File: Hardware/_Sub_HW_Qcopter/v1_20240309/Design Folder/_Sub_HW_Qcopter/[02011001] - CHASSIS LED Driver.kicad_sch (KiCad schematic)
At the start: 2 parts, among them J3201 HDR_1X2_VERT_1.25MM

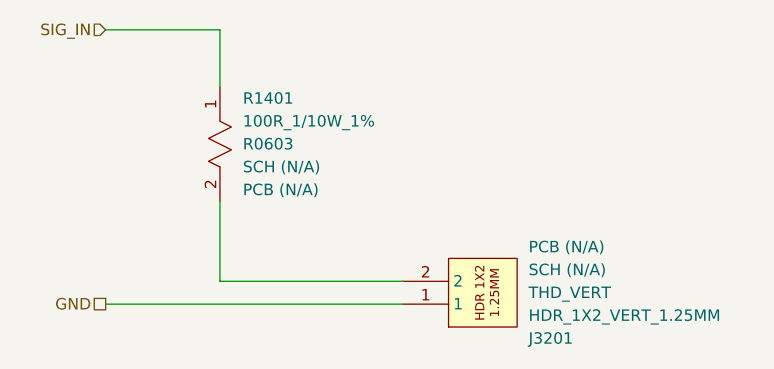
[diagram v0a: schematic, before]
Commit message: Update [02011001] - CHASSIS LED Driver.kicad_sch
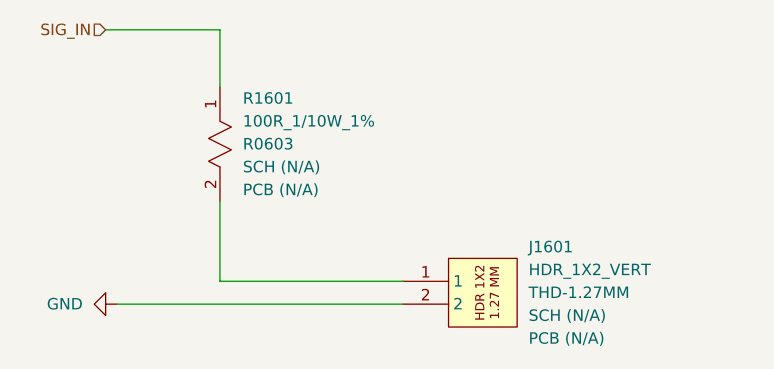
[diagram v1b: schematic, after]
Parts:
- removed J3201: HDR_1X2_VERT_1.25MM, Connector_Hirose:Hirose_DF13-02P-1.25DSA_1x02_P1.25mm_Vertical, symbol _SCHLIB_Qcopter:CONN_HDR_1X2_VERT_THD-1.25MM
- added J1601: HDR_1X2_VERT, Connector_PinHeader_1.27mm:PinHeader_1x02_P1.27mm_Vertical, symbol _SCHLIB_Qcopter:CONN_HDR_1X2_VERT_THD-1.27MM
- renumbered R1401 to R1601
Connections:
- net GND: now also J1601.2
- net at R1601.2: now also J1601.1
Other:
- company: (none) -> Mend0z0
- title: (none) -> Quadcopter
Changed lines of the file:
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@@
 	(paper "C")
 	(title_block
-		(comment 2 "DRAFT")
+		(title "Quadcopter")
+		(date "2024-03-17")
+		(rev "01")
+		(company "Mend0z0")
+		(comment 1 "01")
+		(comment 2 "PRELIMINARY")
+		(comment 3 "Siavash Taher Parvar")
+		(comment 8 "N/A")
+		(comment 9 "First Version")
 	)
 	(wire
@@
 	(wire
 		(pts
-			(xy 241.3 208.28) (xy 274.32 208.28)
+			(xy 254 196.85) (xy 254 205.74)
 		)
 		(stroke
@@
 	(wire
 		(pts
-			(xy 254 196.85) (xy 254 205.74)
+			(xy 241.3 177.8) (xy 254 177.8)
 		)
 		(stroke
@@
 	(wire
 		(pts
-			(xy 241.3 177.8) (xy 254 177.8)
+			(xy 242.57 208.28) (xy 274.32 208.28)
 		)
 		(stroke
 			(width 0)
 			(type default)
-		)
-	)
-	(hierarchical_label "GND"
-		(shape passive)
-		(at 241.3 208.28 180)
-		(fields_autoplaced yes)
-		(effects
-			(font
-				(size 1.27 1.27)
-			)
-			(justify right)
 		)
 	)
@@
 	)
 	(symbol
-		(lib_id "_SCHLIB_Qcopter:CONN_HDR_1X2_VERT_THD-1.25MM")
-		(at 279.4 210.82 0)
-		(mirror x)
+		(lib_id "_SCHLIB_Qcopter:CONN_HDR_1X2_VERT_THD-1.27MM")
+		(at 274.32 205.74 0)
 		(unit 1)
 		(exclude_from_sim no)
@@
 		(on_board yes)
 		(dnp no)
-		(property "Reference" "J3201"
-			(at 288.29 212.0901 0)
-			(effects
-				(font
-					(size 1.27 1.27)
-				)
-				(justify left)
-			)
-		)
-		(property "Value" "HDR_1X2_VERT_1.25MM"
-			(at 288.29 209.5501 0)
-			(effects
-				(font
-					(size 1.27 1.27)
-				)
-				(justify left)
-			)
-		)
-		(property "Footprint" "Connector_Hirose:Hirose_DF13-02P-1.25DSA_1x02_P1.25mm_Vertical"
-			(at 283.21 227.584 0)
-			(effects
-				(font
-					(size 1.27 1.27)
-				)
-				(justify left)
-				(hide yes)
-			)
-		)
-		(property "Datasheet" "https://cdn.amphenol-cs.com/media/wysiwyg/files/documentation/datasheet/boardwiretoboard/bwb_1.25mm_wtb.pdf"
-			(at 282.956 219.964 0)
-			(effects
-				(font
-					(size 1.27 1.27)
-				)
-				(justify left)
-				(hide yes)
-			)
-		)
-		(property "Description" "Connector Header Through Hole 2 position 0.049\" (1.25mm)"
-			(at 282.956 224.79 0)
-			(effects
-				(font
-					(size 1.27 1.27)
-				)
-				(justify left)
-				(hide yes)
-			)
-		)
-		(property "Package" "THD_VERT"
-			(at 288.29 207.0101 0)
-			(effects
-				(font
-					(size 1.27 1.27)
-				)
-				(justify left)
-			)
-		)
-		(property "Part Number (Manufacturer)" "10114829-10102LF"
-			(at 283.21 230.378 0)
-			(effects
-				(font
-					(size 1.27 1.27)
-				)
-				(justify left)
-				(hide yes)
-			)
-		)
-		(property "Manufacturer" "Amphenol ICC (FCI)"
-			(at 283.21 235.204 0)
-			(effects
-				(font
-					(size 1.27 1.27)
-				)
-				(justify left)
-				(hide yes)
-			)
-		)
-		(property "Part Number (Vendor)" "609-4383-2-ND"
-			(at 283.21 232.918 0)
+		(fields_autoplaced yes)
+		(property "Reference" "J1601"
+			(at 288.29 201.9299 0)
+			(effects
+				(font
+					(size 1.27 1.27)
+				)
+				(justify left)
+			)
+		)
+		(property "Value" "HDR_1X2_VERT"
+			(at 288.29 204.4699 0)
+			(effects
+				(font
+					(size 1.27 1.27)
+				)
+				(justify left)
+			)
+		)
+		(property "Footprint" "Connector_PinHeader_1.27mm:PinHeader_1x02_P1.27mm_Vertical"
+			(at 278.13 188.976 0)
+			(effects
+				(font
+					(size 1.27 1.27)
+				)
+				(justify left)
+				(hide yes)
+			)
+		)
+		(property "Datasheet" "https://cdn.harwin.com/pdfs/M50-353.pdf"
+			(at 277.876 196.596 0)
+			(effects
+				(font
+					(size 1.27 1.27)
+				)
+				(justify left)
+				(hide yes)
+			)
+		)
+		(property "Description" "Connector Header Through Hole 2 position 0.050\" (1.27mm)"
+			(at 277.876 191.77 0)
+			(effects
+				(font
+					(size 1.27 1.27)
+				)
+				(justify left)
+				(hide yes)
+			)
+		)
+		(property "Package" "THD-1.27MM"
+			(at 288.29 207.0099 0)
+			(effects
+				(font
+					(size 1.27 1.27)
+				)
+				(justify left)
+			)
+		)
+		(property "Part Number (Manufacturer)" "M50-3530242"
+			(at 278.13 186.182 0)
+			(effects
+				(font
+					(size 1.27 1.27)
+				)
+				(justify left)
+				(hide yes)
+			)
+		)
+		(property "Manufacturer" "Harwin Inc."
+			(at 278.13 181.356 0)
+			(effects
+				(font
+					(size 1.27 1.27)
+				)
+				(justify left)
+				(hide yes)
+			)
+		)
+		(property "Part Number (Vendor)" "952-3598-ND"
+			(at 278.13 183.642 0)
 			(effects
 				(font
@@
 		)
 		(property "Vendor" "Digikey"
-			(at 283.21 237.744 0)
-			(effects
-				(font
-					(size 1.27 1.27)
-				)
-				(justify left)
-				(hide yes)
-			)
-		)
-		(property "Purchase Link" "https://www.digikey.ca/en/products/detail/amphenol-cs-fci/10114829-10102LF/2658929"
-			(at 282.956 222.504 0)
+			(at 278.13 178.816 0)
+			(effects
+				(font
+					(size 1.27 1.27)
+				)
+				(justify left)
+				(hide yes)
+			)
+		)
+		(property "Purchase Link" "https://www.digikey.ca/en/products/detail/harwin-inc/M50-3530242/7044013"
+			(at 277.876 194.056 0)
 			(effects
 				(font
@@
 		)
 		(property "SCH CHECK" "SCH (N/A)"
-			(at 288.29 204.4701 0)
+			(at 288.29 209.5499 0)
 			(effects
 				(font
@@
 		)
 		(property "PCB CHECK" "PCB (N/A)"
-			(at 288.29 201.9301 0)
+			(at 288.29 212.0899 0)
 			(effects
 				(font
@@
 			(project "_Sub_HW_Qcopter"
 				(path "/b8703f06-b3da-4de2-b217-f104939b36e8/6184e84e-040e-4878-8152-76cf0b949e21/e826979f-4a88-401c-bba5-a1c30231907a/18b6f30a-cfd9-47dd-912b-fd9e3d81f3b7/d01f197b-a0f5-41b1-b267-05c3be6c8f44"
-					(reference "J3201")
+					(reference "J1601")
 					(unit 1)
 				)
 				(path "/b8703f06-b3da-4de2-b217-f104939b36e8/6184e84e-040e-4878-8152-76cf0b949e21/e826979f-4a88-401c-bba5-a1c30231907a/18b6f30a-cfd9-47dd-912b-fd9e3d81f3b7/9dfe4c39-4ceb-4fd2-b56a-1baa2fce7dec"
-					(reference "J1401")
+					(reference "J1701")
 					(unit 1)
 				)
 				(path "/b8703f06-b3da-4de2-b217-f104939b36e8/6184e84e-040e-4878-8152-76cf0b949e21/e826979f-4a88-401c-bba5-a1c30231907a/18b6f30a-cfd9-47dd-912b-fd9e3d81f3b7/9b435483-0088-4023-8c4e-fad88eb5f6b4"
-					(reference "J3401")
+					(reference "J1801")
 					(unit 1)
 				)
 				(path "/b8703f06-b3da-4de2-b217-f104939b36e8/6184e84e-040e-4878-8152-76cf0b949e21/e826979f-4a88-401c-bba5-a1c30231907a/18b6f30a-cfd9-47dd-912b-fd9e3d81f3b7/b5f98916-9852-4daa-96f4-3bdba60c13f5"
-					(reference "J3501")
+					(reference "J1901")
+					(unit 1)
+				)
+			)
+		)
+	)
+	(symbol
+		(lib_id "power:GND")
+		(at 242.57 208.28 270)
+		(unit 1)
+		(exclude_from_sim no)
+		(in_bom yes)
+		(on_board yes)
+		(dnp no)
+		(fields_autoplaced yes)
+		(property "Reference" "#PWR01601"
+			(at 236.22 208.28 0)
+			(effects
+				(font
+					(size 1.27 1.27)
+				)
+				(hide yes)
+			)
+		)
+		(property "Value" "GND"
+			(at 238.76 208.2799 90)
+			(effects
+				(font
+					(size 1.27 1.27)
+				)
+				(justify right)
+			)
+		)
+		(property "Footprint" ""
+			(at 242.57 208.28 0)
+			(effects
+				(font
+					(size 1.27 1.27)
+				)
+				(hide yes)
+			)
+		)
+		(property "Datasheet" ""
+			(at 242.57 208.28 0)
+			(effects
+				(font
+					(size 1.27 1.27)
+				)
+				(hide yes)
+			)
+		)
+		(property "Description" "Power symbol creates a global label with name \"GND\" , ground"
+			(at 242.57 208.28 0)
+			(effects
+				(font
+					(size 1.27 1.27)
+				)
+				(hide yes)
+			)
+		)
+		(pin "1"
+		)
+		(instances
+			(project "_Sub_HW_Qcopter"
+				(path "/b8703f06-b3da-4de2-b217-f104939b36e8/6184e84e-040e-4878-8152-76cf0b949e21/e826979f-4a88-401c-bba5-a1c30231907a/18b6f30a-cfd9-47dd-912b-fd9e3d81f3b7/d01f197b-a0f5-41b1-b267-05c3be6c8f44"
+					(reference "#PWR01601")
+					(unit 1)
+				)
+				(path "/b8703f06-b3da-4de2-b217-f104939b36e8/6184e84e-040e-4878-8152-76cf0b949e21/e826979f-4a88-401c-bba5-a1c30231907a/18b6f30a-cfd9-47dd-912b-fd9e3d81f3b7/9dfe4c39-4ceb-4fd2-b56a-1baa2fce7dec"
+					(reference "#PWR01701")
+					(unit 1)
+				)
+				(path "/b8703f06-b3da-4de2-b217-f104939b36e8/6184e84e-040e-4878-8152-76cf0b949e21/e826979f-4a88-401c-bba5-a1c30231907a/18b6f30a-cfd9-47dd-912b-fd9e3d81f3b7/9b435483-0088-4023-8c4e-fad88eb5f6b4"
+					(reference "#PWR01801")
+					(unit 1)
+				)
+				(path "/b8703f06-b3da-4de2-b217-f104939b36e8/6184e84e-040e-4878-8152-76cf0b949e21/e826979f-4a88-401c-bba5-a1c30231907a/18b6f30a-cfd9-47dd-912b-fd9e3d81f3b7/b5f98916-9852-4daa-96f4-3bdba60c13f5"
+					(reference "#PWR01901")
 					(unit 1)
 				)
@@
 		(dnp no)
 		(fields_autoplaced yes)
-		(property "Reference" "R1401"
+		(property "Reference" "R1601"
 			(at 256.54 185.4199 90)
 			(effects
@@
 		(instances
 			(project "_Sub_HW_Qcopter"
+				(path "/b8703f06-b3da-4de2-b217-f104939b36e8/6184e84e-040e-4878-8152-76cf0b949e21/e826979f-4a88-401c-bba5-a1c30231907a/18b6f30a-cfd9-47dd-912b-fd9e3d81f3b7/d01f197b-a0f5-41b1-b267-05c3be6c8f44"
+					(reference "R1601")
+					(unit 1)
+				)
 				(path "/b8703f06-b3da-4de2-b217-f104939b36e8/6184e84e-040e-4878-8152-76cf0b949e21/e826979f-4a88-401c-bba5-a1c30231907a/18b6f30a-cfd9-47dd-912b-fd9e3d81f3b7/9dfe4c39-4ceb-4fd2-b56a-1baa2fce7dec"
-					(reference "R1401")
+					(reference "R1701")
 					(unit 1)
 				)
 				(path "/b8703f06-b3da-4de2-b217-f104939b36e8/6184e84e-040e-4878-8152-76cf0b949e21/e826979f-4a88-401c-bba5-a1c30231907a/18b6f30a-cfd9-47dd-912b-fd9e3d81f3b7/9b435483-0088-4023-8c4e-fad88eb5f6b4"
-					(reference "R3401")
+					(reference "R1801")
 					(unit 1)
 				)
 				(path "/b8703f06-b3da-4de2-b217-f104939b36e8/6184e84e-040e-4878-8152-76cf0b949e21/e826979f-4a88-401c-bba5-a1c30231907a/18b6f30a-cfd9-47dd-912b-fd9e3d81f3b7/b5f98916-9852-4daa-96f4-3bdba60c13f5"
-					(reference "R3501")
-					(unit 1)
-				)
-				(path "/b8703f06-b3da-4de2-b217-f104939b36e8/6184e84e-040e-4878-8152-76cf0b949e21/e826979f-4a88-401c-bba5-a1c30231907a/18b6f30a-cfd9-47dd-912b-fd9e3d81f3b7/d01f197b-a0f5-41b1-b267-05c3be6c8f44"
-					(reference "R3201")
-					(unit 1)
-				)
+					(reference "R1901")
+					(unit 1)
+				)
